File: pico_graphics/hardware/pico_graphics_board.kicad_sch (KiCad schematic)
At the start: 6 parts, among them J1 8bit_thing_bus_connector, J2 HDMI_A, U1 Pico, U2 SLG46826G, U3 74LVC245, U4 74LVC245

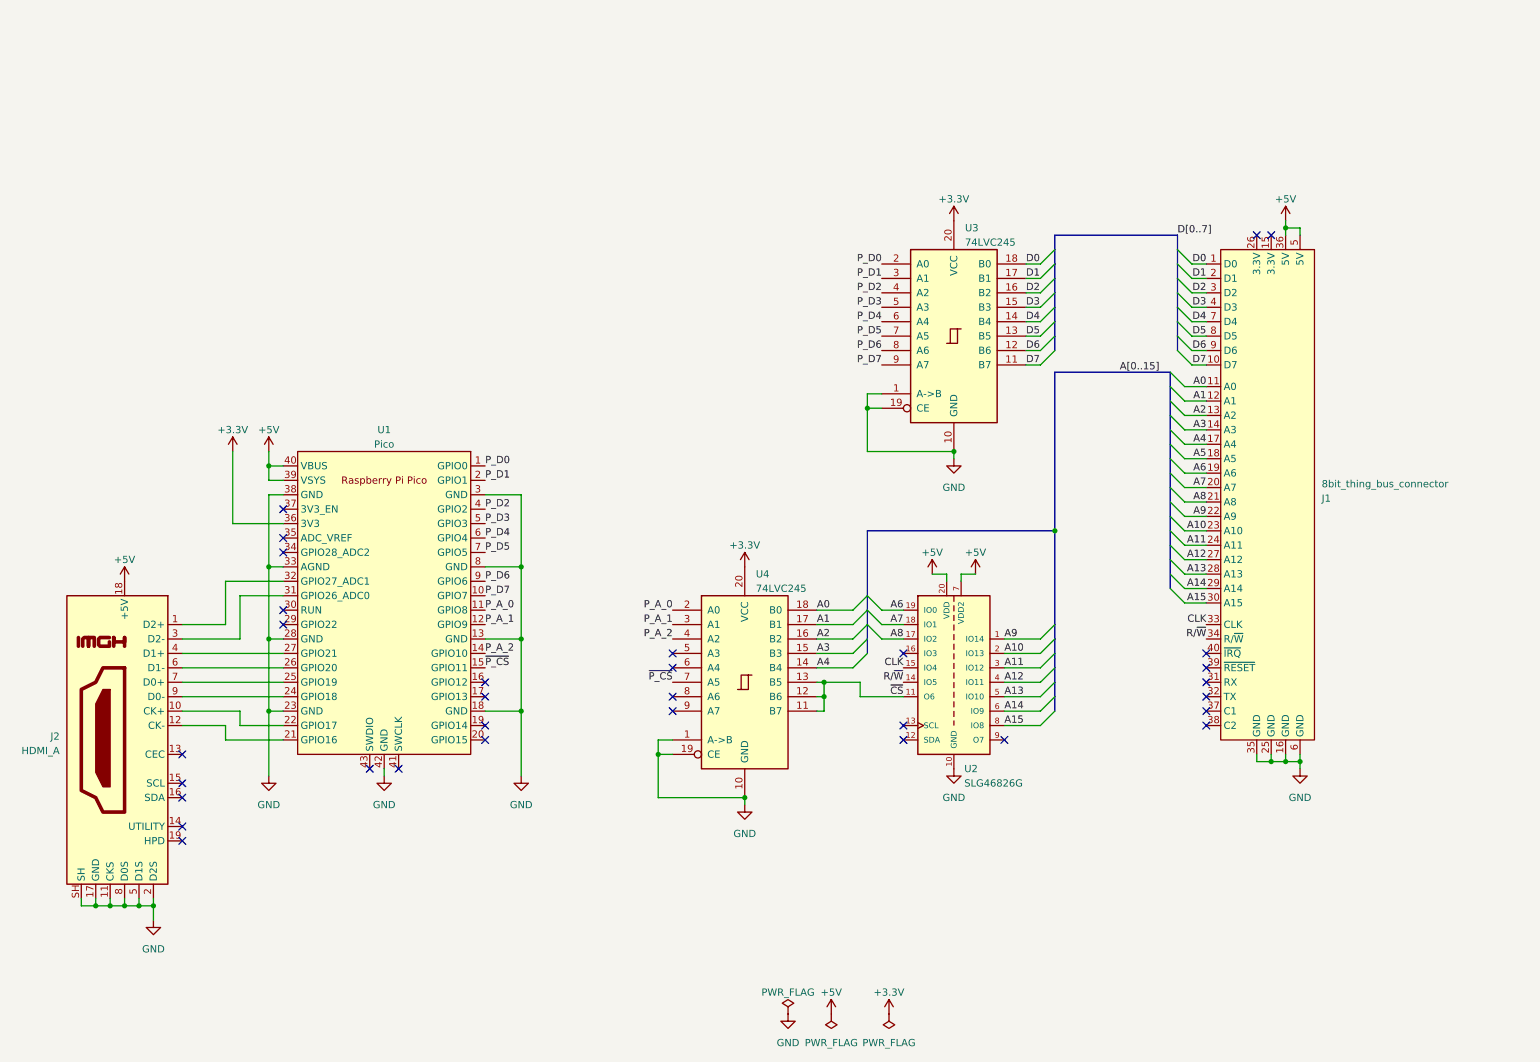
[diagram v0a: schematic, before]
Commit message: Schematic and routed board for pico graphics
The board is looking good, but we moved quite a few pins around to make routing
easier. This needs testing before sending it to be manufactured.
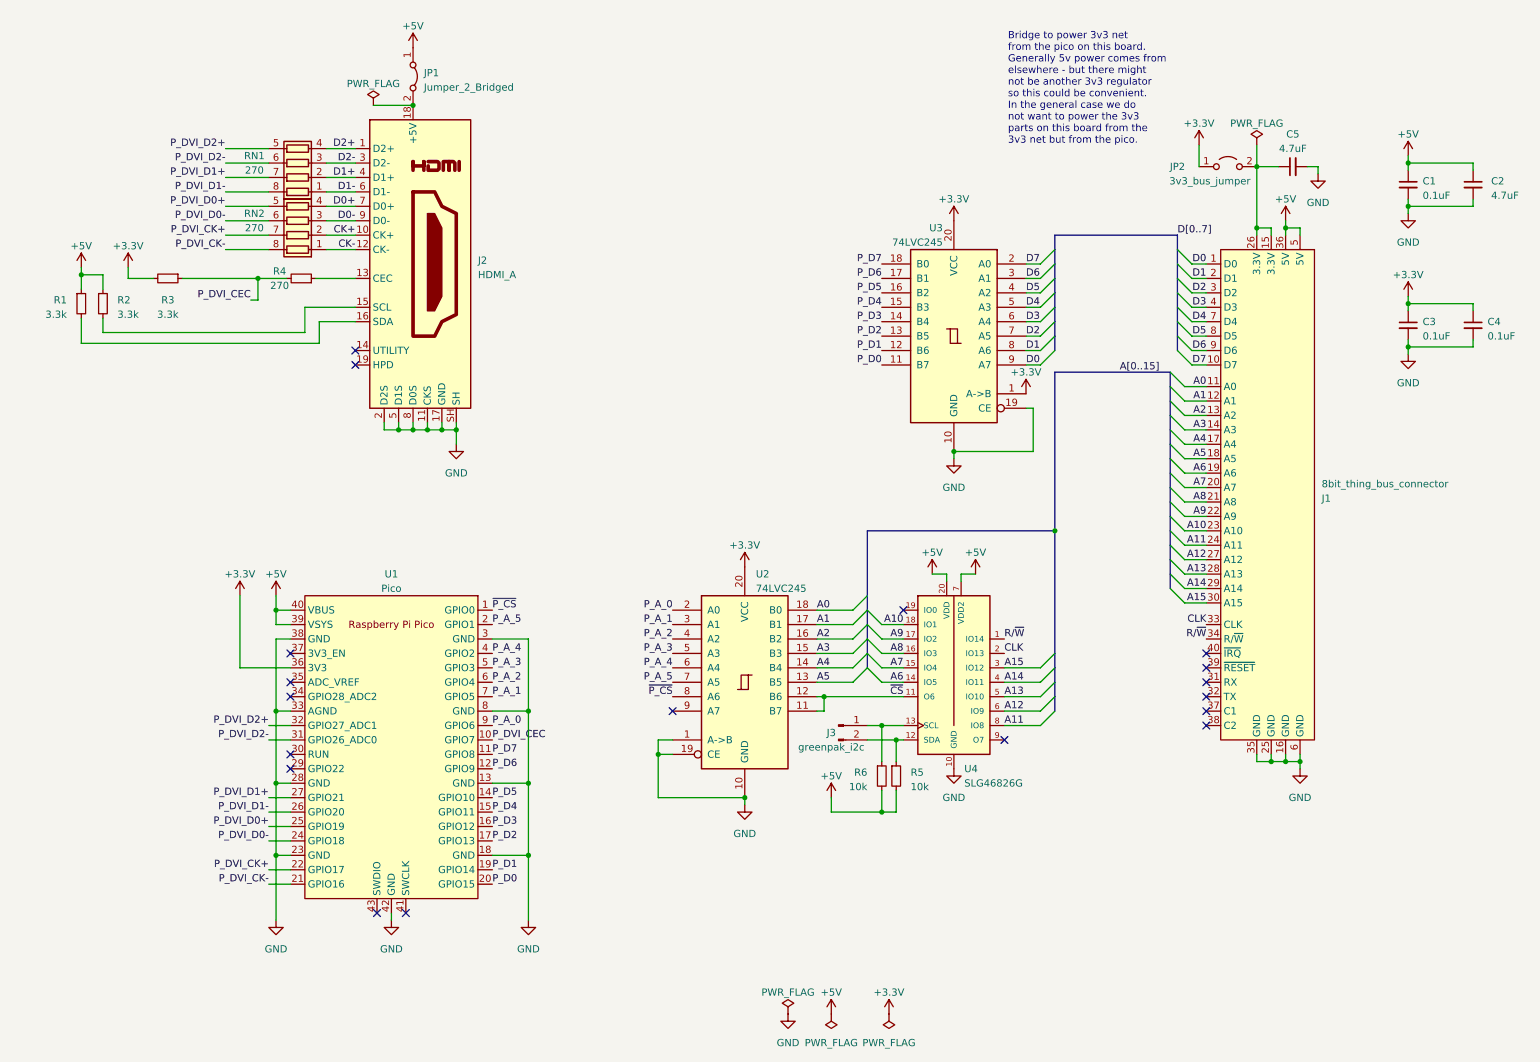
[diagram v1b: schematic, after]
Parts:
- added C1, C3, C4: 0.1uF, Capacitor_SMD:C_0805_2012Metric_Pad1.18x1.45mm_HandSolder, symbol Device:C_Small
- added C2, C5: 4.7uF, Capacitor_SMD:C_0805_2012Metric_Pad1.18x1.45mm_HandSolder, symbol Device:C_Small
- added J3: greenpak_i2c, own_footprints:PinHeader_1x02_P2.54mm_Vertical_minimal, symbol Connector:Conn_01x02_Pin
- added JP1: Jumper_2_Bridged, Resistor_SMD:R_0805_2012Metric_Pad1.20x1.40mm_HandSolder, symbol Jumper:Jumper_2_Bridged
- added JP2: 3v3_bus_jumper, own_footprints:PinHeader_1x02_P2.54mm_Vertical_minimal, symbol Jumper:Jumper_2_Open
- added R1, R2, R3: 3.3k, Resistor_SMD:R_0805_2012Metric_Pad1.20x1.40mm_HandSolder, symbol Device:R_Small
- added R4: 270, Resistor_SMD:R_0805_2012Metric_Pad1.20x1.40mm_HandSolder, symbol Device:R_Small
- added R5, R6: 10k, Resistor_SMD:R_0805_2012Metric_Pad1.20x1.40mm_HandSolder, symbol Device:R_Small
- added RN1, RN2: 270, Resistor_SMD:R_Array_Convex_4x1206, symbol Device:R_Pack04
- J2: footprint (none) -> Connector_HDMI:HDMI_A_Amphenol_10029449-x01xLF_Horizontal
- U1: footprint RPi_Pico:RPi_Pico_SMD_TH -> imported_footprints:RPi_Pico_SMD_TH
- U2: renamed from U4; footprint (none) -> Package_SO:TSSOP-20_4.4x6.5mm_P0.65mm
- U3: footprint (none) -> Package_SO:TSSOP-20_4.4x6.5mm_P0.65mm
- U4: renamed from U2; footprint SOP65P640X120-20N -> Package_SO:TSSOP-20_4.4x6.5mm_P0.65mm
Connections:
- net +3.3V: now also U3.1 (A->B), C3.1, C4.1, JP2.1 (A), R3.2
- net +5V: now also C1.1, C2.1, JP1.1 (A), R1.1, R2.1, R5.2, R6.2; no longer J2.18 (+5V)
- net A10: now also U4.18 (IO1); no longer U4.2 (IO13)
- net A11: now also U4.8 (IO8); no longer U4.3 (IO12)
- net A12: now also U4.6 (IO9); no longer U4.4 (IO11)
- net A14: now also U4.4 (IO11); no longer U4.6 (IO9)
- net A15: now also U4.3 (IO12); no longer U4.8 (IO8)
- net A5: now also U2.13 (B5)
- net A6: now also U4.14 (IO5); no longer U4.19 (IO0)
- net A7: now also U4.15 (IO4); no longer U4.18 (IO1)
- net A8: now also U4.16 (IO3); no longer U4.17 (IO2)
- net A9: now also U4.17 (IO2); no longer U4.1 (IO14)
- net CLK: now also U4.2 (IO13); no longer U4.15 (IO4)
- net D0: now also U3.9 (A7); no longer U3.18 (B0)
- net D1: now also U3.8 (A6); no longer U3.17 (B1)
- net D2: now also U3.7 (A5); no longer U3.16 (B2)
- net D3: now also U3.6 (A4); no longer U3.15 (B3)
- net D4: now also U3.5 (A3); no longer U3.14 (B4)
- net D5: now also U3.4 (A2); no longer U3.13 (B5)
- net D6: now also U3.3 (A1); no longer U3.12 (B6)
- net D7: now also U3.2 (A0); no longer U3.11 (B7)
- net GND: now also C1.2, C2.2, C3.2, C4.2, C5.2; no longer U3.1 (A->B)
- net P_A_0: now also U1.9 (GPIO6); no longer U1.11 (GPIO8)
- net P_A_1: now also U1.7 (GPIO5); no longer U1.12 (GPIO9)
- net P_A_2: now also U1.6 (GPIO4); no longer U1.14 (GPIO10)
- net P_D0: now also U1.20 (GPIO15), U3.11 (B7); no longer U1.1 (GPIO0), U3.2 (A0)
- net P_D1: now also U1.19 (GPIO14), U3.12 (B6); no longer U1.2 (GPIO1), U3.3 (A1)
- net P_D2: now also U1.17 (GPIO13), U3.13 (B5); no longer U1.4 (GPIO2), U3.4 (A2)
- net P_D3: now also U1.16 (GPIO12), U3.14 (B4); no longer U1.5 (GPIO3), U3.5 (A3)
- net P_D4: now also U1.15 (GPIO11), U3.15 (B3); no longer U1.6 (GPIO4), U3.6 (A4)
- net P_D5: now also U1.14 (GPIO10), U3.16 (B2); no longer U1.7 (GPIO5), U3.7 (A5)
- net P_D6: now also U1.12 (GPIO9), U3.17 (B1); no longer U1.9 (GPIO6), U3.8 (A6)
- net P_D7: now also U1.11 (GPIO8), U3.18 (B0); no longer U1.10 (GPIO7), U3.9 (A7)
- net R/~{W}: now also U4.1 (IO14); no longer U4.14 (IO5)
- net ~{CS}: no longer U2.13 (B5)
- net ~{P_CS}: now also U1.1 (GPIO0), U2.8 (A6); no longer U1.15 (GPIO11), U2.7 (A5)
- net P_A_3: now reaches U2.5 (A3)
- net P_A_3: now also U1.5 (GPIO3)
- net P_A_4: now reaches U2.6 (A4)
- net P_A_4: now also U1.4 (GPIO2)
- net CK-: now reaches J2.12 (CK-)
- net CK-: now also RN2.1 (R1.1); no longer U1.21 (GPIO16)
- net CK+: now reaches J2.10 (CK+)
- net CK+: now also RN2.2 (R2.1); no longer U1.22 (GPIO17)
- net D0-: now reaches J2.9 (D0-)
- net D0-: now also RN2.3 (R3.1); no longer U1.24 (GPIO18)
- net D0+: now reaches J2.7 (D0+)
- net D0+: now also RN2.4 (R4.1); no longer U1.25 (GPIO19)
- net D1-: now reaches J2.6 (D1-)
- net D1-: now also RN1.1 (R1.1); no longer U1.26 (GPIO20)
- net D1+: now reaches J2.4 (D1+)
- net D1+: now also RN1.2 (R2.1); no longer U1.27 (GPIO21)
- net D2-: now reaches J2.3 (D2-)
- net D2-: now also RN1.3 (R3.1); no longer U1.31 (GPIO26_ADC0)
- net D2+: now reaches J2.1 (D2+)
- net D2+: now also RN1.4 (R4.1); no longer U1.32 (GPIO27_ADC1)
- net at J2.13 (CEC): now also R4.1
- net at J2.15 (SCL): now also R2.2
- net at J2.16 (SDA): now also R1.2
- net at J1.15 (3.3V): now also J1.26 (3.3V), C5.1, JP2.2 (B)
- net at U4.12 (SDA): now also J3.2 (Pin_2), R5.1
- net at U4.13 (SCL): now also J3.1 (Pin_1), R6.1
- new net: J2.18 (+5V), JP1.2 (B)
- new net P_A_5: U1.2 (GPIO1), U2.7 (A5)
- new net P_DVI_CEC: R3.1, R4.2, U1.10 (GPIO7)
- new net P_DVI_CK+: RN2.7 (R2.2), U1.22 (GPIO17)
- new net P_DVI_CK-: RN2.8 (R1.2), U1.21 (GPIO16)
- new net P_DVI_D0+: RN2.5 (R4.2), U1.25 (GPIO19)
- new net P_DVI_D0-: RN2.6 (R3.2), U1.24 (GPIO18)
- new net P_DVI_D1+: RN1.7 (R2.2), U1.27 (GPIO21)
- new net P_DVI_D1-: RN1.8 (R1.2), U1.26 (GPIO20)
- new net P_DVI_D2+: RN1.5 (R4.2), U1.32 (GPIO27_ADC1)
- new net P_DVI_D2-: RN1.6 (R3.2), U1.31 (GPIO26_ADC0)
- no-connect marks 32 -> 18
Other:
- note added: "Bridge to power 3v3 net from the pico on this board. Generally 5v power comes from elsewhere - but there might not be another 3v3 regulator so this could be convenient. In the general case we do not want to power the 3v3 parts on this board from the 3v3 net but from the pico."
- moved on the sheet: J2, U1

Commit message: Fix resistor network footprint size
Kicad footprints are confusingly labeled by the individual resistor size as
opposed to the size of the full package - so 4x1206 means 'as big as 4x 1206
resistors' not as big as one 1206 as is used in manufacturers' datasheets.
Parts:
- RN1, RN2: footprint Resistor_SMD:R_Array_Convex_4x1206 -> Resistor_SMD:R_Array_Concave_4x0603
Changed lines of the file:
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@@
       (effects (font (size 1.27 1.27)))
     )
-    (property "Footprint" "Resistor_SMD:R_Array_Convex_4x1206" (at 66.04 42.545 90)
+    (property "Footprint" "Resistor_SMD:R_Array_Concave_4x0603" (at 66.04 42.545 90)
       (effects (font (size 1.27 1.27)) hide)
     )
@@
       (effects (font (size 1.27 1.27)))
     )
-    (property "Footprint" "Resistor_SMD:R_Array_Convex_4x1206" (at 66.04 32.385 90)
-      (effects (font (size 1.27 1.27)) hide)
-    )
+    (property "Footprint" "Resistor_SMD:R_Array_Concave_4x0603" (at 66.04 32.385 90)
+      (effects (font (size 1.27 1.27)) hide)
+    )

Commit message: Final pico graphics v1.0 board
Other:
- moved on the sheet: C1, C2, C3, C4, C5, J1, J2, J3, JP1, JP2, R1, R2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
